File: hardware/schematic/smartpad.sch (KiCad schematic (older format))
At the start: 53 parts, among them CN2 Conn_01x04, J1 USB_B_Mini, Q1 DMG2301L, Q2 DMG2301L, Q3 DMG2301L, Q4 DMG2301L, Q5 DMG2301L, Q6 DMG2301L, Q7 DMG2301L, Q8 DMG2301L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

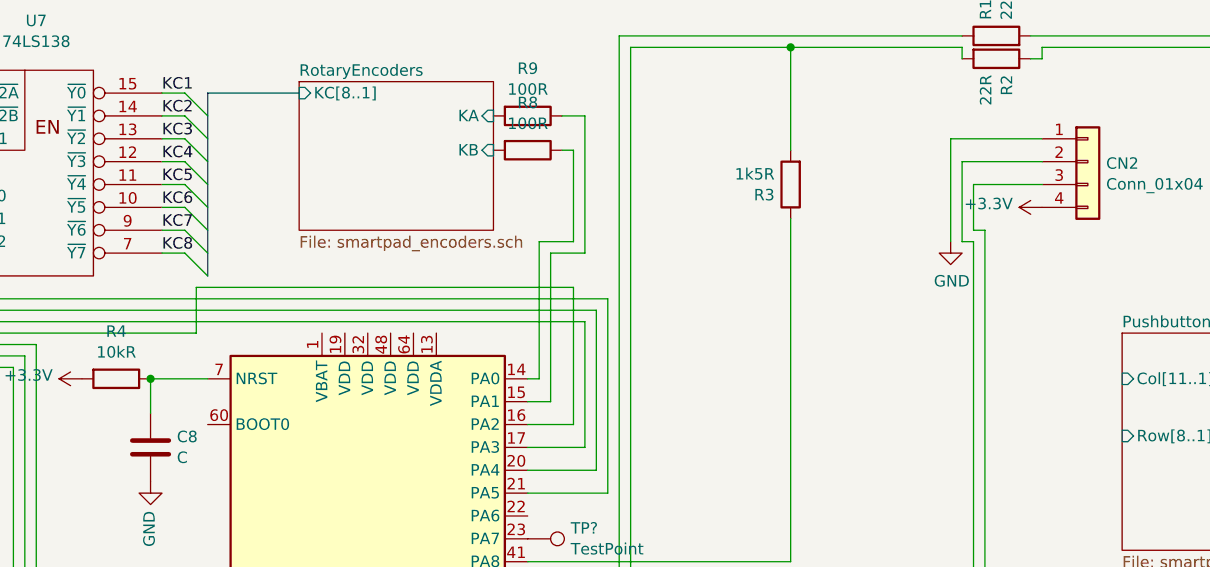
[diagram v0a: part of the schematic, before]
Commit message: Connect NRST to corresponding pin. (Fixes #3)
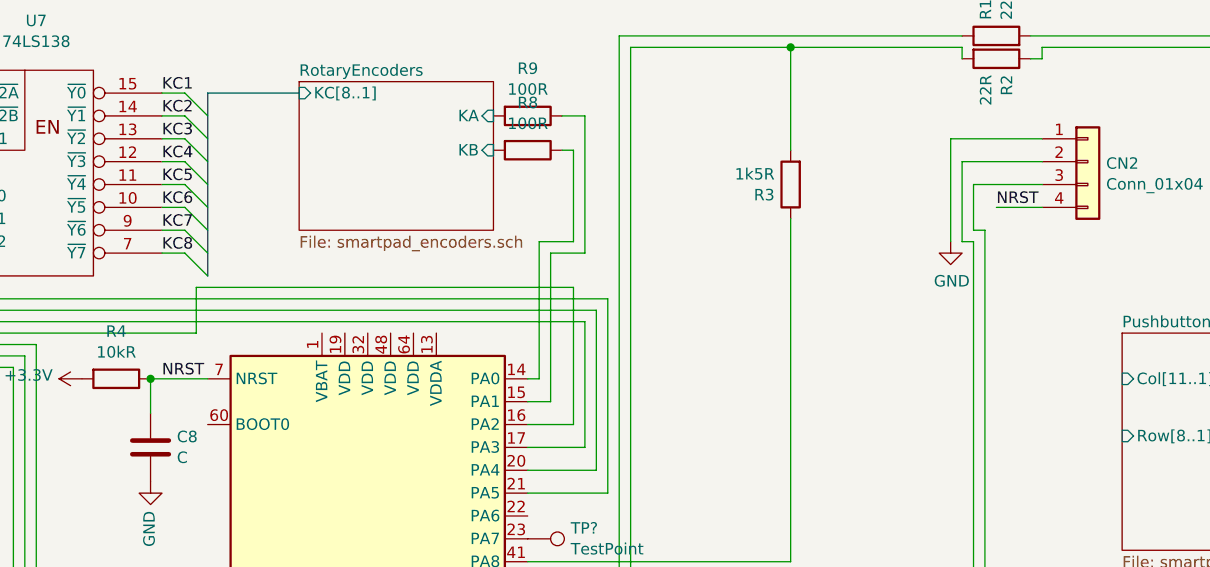
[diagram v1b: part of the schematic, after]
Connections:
- net +3V3: no longer CN2.4 (Pin_4)
- net NRST: now reaches C8.1, R4.1, U2.7 (NRST)
- net NRST: now also CN2.4 (Pin_4)
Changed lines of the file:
@@
 EESchema Schematic File Version 4
-LIBS:smartpad-cache
-EELAYER 29 0
+EELAYER 30 0
 EELAYER END
 $Descr A4 11693 8268
@@
 F 3 "" H 4100 1150 50  0001 C CNN
 	1    4100 1150
-	0    -1   -1   0
-$EndComp
-$Comp
-L power:+3.3V #PWR0120
-U 1 1 5D318EF6
-P 9050 1450
-F 0 "#PWR0120" H 9050 1300 50  0001 C CNN
-F 1 "+3.3V" V 9065 1578 50  0000 L CNN
-F 2 "" H 9050 1450 50  0001 C CNN
-F 3 "" H 9050 1450 50  0001 C CNN
-	1    9050 1450
 	0    -1   -1   0
 $EndComp
@@
 	0    1    1    0
 $EndComp
+Text Notes 8150 3850 0    50   ~ 0
+LED driver output routing is yet to be inspected
+Text Label 5200 2200 0    50   ~ 0
+NRST
+Wire Wire Line
+	9050 1450 8850 1450
 Wire Bus Line
 	5400 950  5400 1750
-Text Notes 8150 3850 0    50   ~ 0
-LED driver output routing is yet to be inspected
+Text Label 8850 1450 0    50   ~ 0
+NRST
 $EndSCHEMATC
